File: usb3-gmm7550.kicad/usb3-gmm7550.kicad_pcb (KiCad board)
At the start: 4 copper layers, 75 x 50 mm, 209 parts, among them J1 USB_C_Receptacle, J2 USB_C_Receptacle_USB2.0, J3 SWD, J4 10144517-061802LF, J5 10144517-061802LF, J6 DNI, Q1 NX6008NBK, Q2 NX6008NBK, Q3 NX6008NBK, Q4 STL9P3LLH6, Q5 STL9P3LLH6, Q6 STL9P3LLH6, Q7 NX6008NBK, SW1 SW_Push, SW2 SW_Push, SW3 SW_Push, SW4 SW_Push, SW5 SW_Push, SW6 SW_DIP_x02, U1 ECMF4-40A100N10, U10 74LVC1G07, U11 INA180A2, U12 AP7330, U13 AP7330, U14 MX25R1635FZU, U15 ECMF02-2AMX6, U16 LM4040DBZ-3, U17 RP2040, U18 STUSB1600, U19 LM66200DRLR, U2 ECMF4-40A100N10, U3 ECMF02-2AMX6, U4 AP7330, U5 TUSB542, U6 SN65LVDS4RSER, U7 USB3340, U8 STUSB03E, U9 SiP32510, Y1 445I23D12M00000

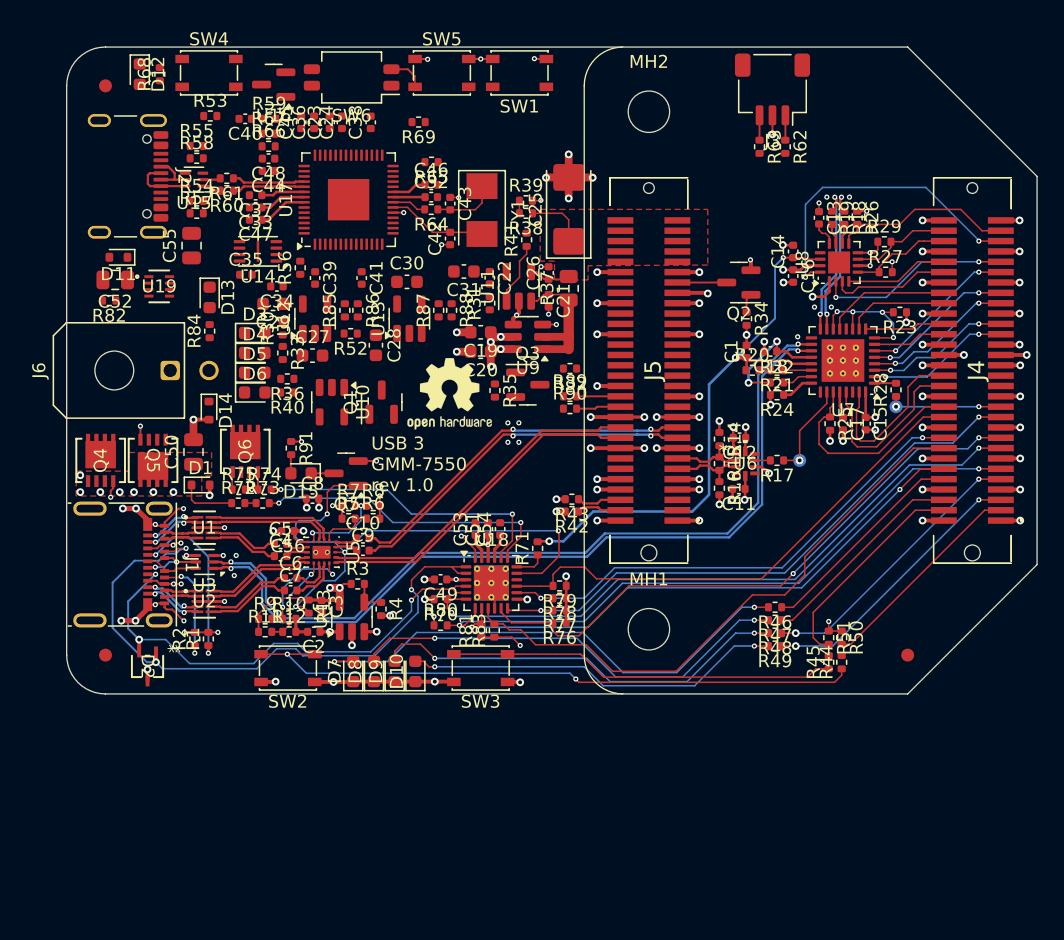
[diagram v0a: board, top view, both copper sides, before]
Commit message: USB Power Delivery redesign (STmicro controller is NRND)
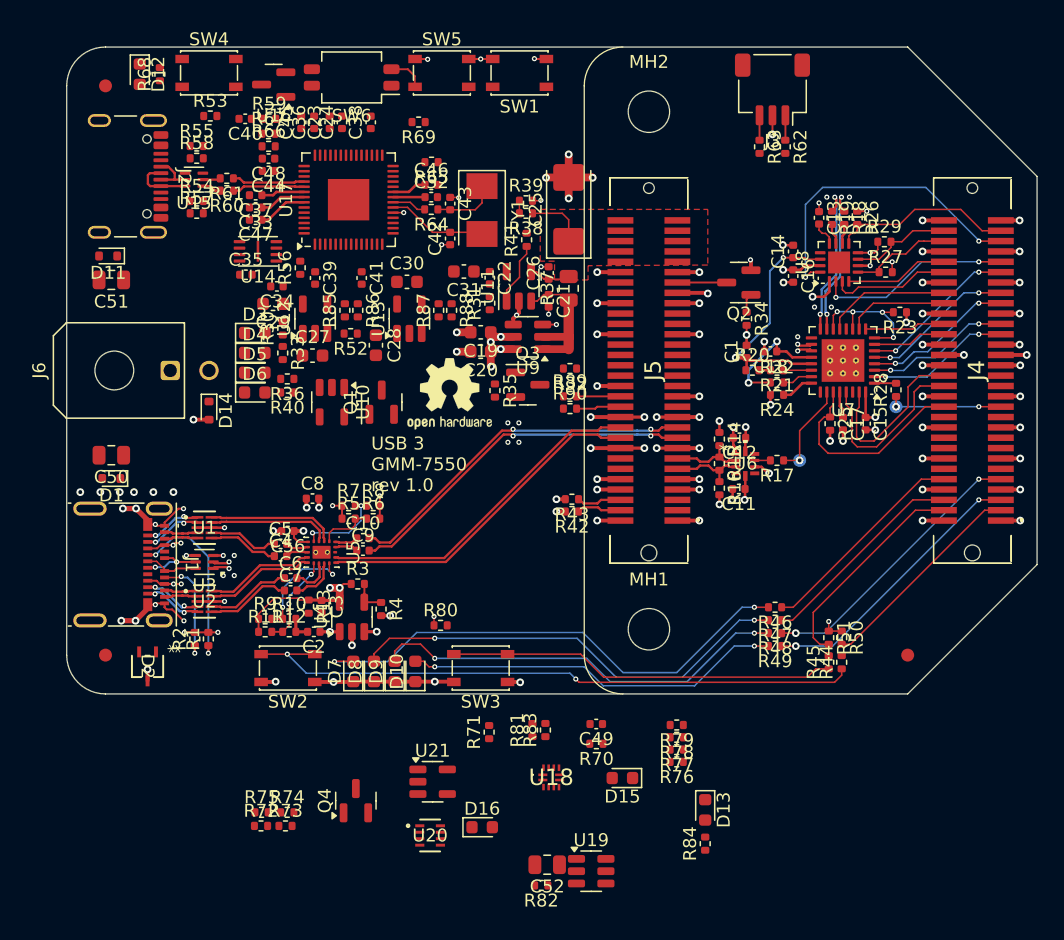
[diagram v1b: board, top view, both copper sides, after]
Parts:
- removed C53, C54: 1.0uF, Capacitor_SMD:C_0402_1005Metric
- removed C55: 10uF, Capacitor_SMD:C_0805_2012Metric
- removed Q5, Q6: STL9P3LLH6, usb3-gmm7550:POWERFLAT_3P3X3P3_STM
- removed Q7: NX6008NBK, Package_TO_SOT_SMD:SOT-23
- removed R91: 100, Resistor_SMD:R_0402_1005Metric
- added D16: 150060VS55040, LED_SMD:LED_0603_1608Metric, F.Cu at (92.1, 110.3)
- added U20: LM66200DRLR, usb3-gmm7550:SOT-5X3_DRL_TEX, F.Cu at (88.1, 110.9)
- added U21: 74LVC1G06, Package_TO_SOT_SMD:SOT-23-5, F.Cu at (88.3, 106.8)
- C51: value 1.0uF -> 10uF; footprint Capacitor_SMD:C_0402_1005Metric -> Capacitor_SMD:C_0805_2012Metric
- Q4: value STL9P3LLH6 -> NX6008NBK; footprint usb3-gmm7550:POWERFLAT_3P3X3P3_STM -> Package_TO_SOT_SMD:SOT-23
- R70: value 1k -> 10k
- R71: value 0 -> 10k
- R75: value 10k -> 1k
- R79: value 10k -> DNI
- R80: value 10k -> 0
- R81: value 10k -> 900k
- R82: value 0 -> 301
- R83: value 10k -> 100
- U18: value STUSB1600 -> FUSB303BTMX; footprint Package_DFN_QFN:QFN-24-1EP_4x4mm_P0.5mm_EP2.7x2.7mm_ThermalVias -> usb3-gmm7550:OnSemi_X2QFN-12_1.6x1.6mm
- U19: value LM66200DRLR -> SiP32508DT; footprint usb3-gmm7550:SOT-5X3_DRL_TEX -> Package_TO_SOT_SMD:TSOT-23-6
- moved C52 56.2 mm to (97.1, 113.2)
- moved R82 56.2 mm to (96.7, 114.8)
- moved U19 56.2 mm to (100.5, 113.7)
- moved D13 55.1 mm to (109.3, 109.0)
- moved R84 55.1 mm to (109.3, 111.6)
- moved C51 34.9 mm to (63.5, 68.0), turned to 180 degrees
- moved D15 34.2 mm to (103.0, 106.5)
- moved Q4 32.9 mm to (82.3, 108.2)
- moved R72 25.0 mm to (75.0, 110.2)
- moved R73 25.0 mm to (76.9, 110.2)
- moved R74 25.0 mm to (77.0, 109.2)
- moved R75 25.0 mm to (75.1, 109.2)
- moved C49 16.4 mm to (100.9, 102.3)
- moved R70 16.4 mm to (100.9, 103.8)
- moved U18 15.7 mm to (97.5, 106.5)
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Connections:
- C49 pad 1: +5V -> +3.3V
- C51 pad 1: +5V -> VBUS_INST
- C52 pad 1: VBUS_INST -> +5V
- D15 pad 1: Net-(D15-K) -> /USB PD/PD_SRC
- J4 pad 15: PD_RESET -> PD_EN_N
- Q4 pad 1: VBUS_TRGT -> PD_DIS
- Q4 pad 2: VBUS_TRGT -> GND
- Q4 pad 3: VBUS_TRGT -> Net-(Q4-D)
- R70 pad 1: PD_RESET -> PD_SRC_EN
- R71 pad 1: Net-(U18-VBUS_SENSE) -> VIO_2V5
- R71 pad 2: VBUS_TRGT -> PD_EN_N
- R72 pad 1: VBUS_TRGT -> PD_DIS
- R72 pad 2: Net-(Q4-G) -> GND
- R73 pad 1: Net-(Q4-G) -> VBUS_TRGT
- R73 pad 2: Net-(U18-VBUS_EN_SNK) -> Net-(Q4-D)
- R74 pad 1: Net-(Q5-G) -> VBUS_TRGT
- R74 pad 2: Net-(U18-VBUS_EN_SRC) -> Net-(Q4-D)
- R75 pad 1: Net-(Q5-S) -> VBUS_TRGT
- R75 pad 2: Net-(Q5-G) -> Net-(Q4-D)
- R76 pad 2: PD_VBUS_VALID -> PD_ALERT_N
- R77 pad 2: PD_ATTACH -> PD_SDA
- R78 pad 2: PD_DEBUG1 -> PD_SCL
- R79 pad 1: VIO_2V5 -> Net-(U18-PORT/DEBUG_N)
- R79 pad 2: PD_DEBUG2 -> GND
- R80 pad 1: VIO_2V5 -> Net-(U20-~{ON})
- R80 pad 2: PD_SCL -> GND
- R81 pad 1: VIO_2V5 -> GND
- R81 pad 2: PD_SDA -> Net-(U18-ADDR/ORIENT)
- R82 pad 1: Net-(U19-~{ON}) -> +5V
- R82 pad 2: GND -> Net-(D13-A)
- R83 pad 1: VIO_2V5 -> +3.3V
- R83 pad 2: PD_ALERT_N -> Net-(D15-A)
- R84 pad 2: Net-(D13-A) -> Net-(D16-A)
- U18 pad 11: PD_VBUS_VALID -> PD_EN_N
- U18 pad 12: PD_ATTACH -> +3.3V
- U18 pad 2: CON_CC1 -> CON_CC2
- U18 pad 3: +5V -> Net-(U18-PORT/DEBUG_N)
- U18 pad 4: CON_CC2 -> VBUS_TRGT
- U18 pad 5: CON_CC2 -> Net-(U18-ADDR/ORIENT)
- U18 pad 6: PD_RESET -> PD_ALERT_N
- U18 pad 7: PD_SCL -> PD_SDA
- U18 pad 8: PD_SDA -> PD_SCL
- U18 pad 9: PD_ALERT_N -> /USB PD/PD_SRC
- U19 pad 1: GND -> VBUS_TRGT
- U19 pad 2: +5V -> VBUS_TRGT
- U19 pad 3: VBUS_INST -> PD_SRC_EN
- U19 pad 4: Net-(U19-~{ON}) -> GND
- U19 pad 5: GND -> +5V
- U19 pad 6: Net-(Q4-D) -> +5V
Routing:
- net USB2_D_P: track 63.8 -> 2.45 mm
- net USB2_D_N: track 63.8 -> 2.45 mm
- net PD_RESET: track 50.6 -> 0.00 mm, vias 2 -> 0
- net PD_SCL: track 49.9 -> 0.00 mm, vias 2 -> 0
- net CON_CC1: track 48.7 -> 0.00 mm, vias 3 -> 0
- net PD_VBUS_VALID: track 46.4 -> 0.00 mm, vias 2 -> 0
- net PD_ALERT_N: track 45.6 -> 0.00 mm
- net PD_ATTACH: track 45.3 -> 0.00 mm, vias 2 -> 0
- net A_B_SIDE: track 43.8 -> 0.00 mm, vias 4 -> 0
- net PD_SDA: track 43.6 -> 0.00 mm, vias 2 -> 0
- net PD_DEBUG2: track 39.7 -> 0.00 mm
- net PD_DEBUG1: track 39.3 -> 0.00 mm, vias 2 -> 0
- net CON_CC2: track 38.5 -> 0.00 mm, vias 3 -> 0
- net VBUS_TRGT: track 57.7 -> 24.7 mm, vias 15 -> 12
- net Net-(U18-VBUS_EN_SNK): track 23.5 -> 0.00 mm, vias 2 -> 0
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- removed copper zone on F.Cu, net VBUS_TRGT

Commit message: Layout WIP: split power plane (internal layer 2)
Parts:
- added C53: 1.0uF, Capacitor_SMD:C_0402_1005Metric, F.Cu at (70.8, 82.2)
- moved C52 53.5 mm to (71.0, 66.5), turned to 90 degrees
- moved D13 53.5 mm to (72.9, 69.8), turned to 180 degrees
- moved R82 52.1 mm to (70.4, 69.8), turned to 0 degrees
- moved U20 48.0 mm to (67.2, 67.8)
- moved R84 47.1 mm to (72.5, 82.2), turned to -90 degrees
- moved U19 45.5 mm to (68.2, 81.7)
- moved R70 37.8 mm to (68.8, 84.0), turned to 0 degrees
- moved R80 33.3 mm to (66.9, 69.8)
- moved D16 33.0 mm to (71.8, 84.3)
- moved R72 32.0 mm to (78.0, 78.3), turned to 90 degrees
- moved Q4 29.3 mm to (75.5, 79.8), turned to -90 degrees
- moved R73 26.7 mm to (75.0, 83.6)
- moved R75 26.6 mm to (75.0, 82.6)
- moved R74 24.6 mm to (75.0, 84.6)
- moved D15 19.0 mm to (95.6, 89.0)
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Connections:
- D2 pad 1: CON_CC1 -> CON_CC2
- D2 pad 2: CON_CC2 -> CON_CC1
- J4 pad 17: PD_VBUS_VALID -> IO_SB_A5
- J4 pad 18: PD_DEBUG1 -> IO_SB_A1
- J4 pad 21: PD_ATTACH -> PD_SRC_EN
- J4 pad 22: PD_DEBUG2 -> PD_DISCH
- Q4 pad 1: PD_DIS -> PD_DISCH
- R72 pad 1: PD_DIS -> PD_DISCH
- U17 pad 35: IO_SB_A7 -> IO_SB_A5
- U17 pad 36: IO_SB_B7 -> IO_SB_A1
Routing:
- net VBUS_TRGT: track 24.7 -> 113.4 mm, vias 12 -> 15
- net GND: track 143.8 -> 220.9 mm, vias 110 -> 172
- net USB2_D_P: track 2.45 -> 65.7 mm
- net USB2_D_N: track 2.45 -> 65.7 mm
- net CON_CC2: track 0.00 -> 35.0 mm, vias 0 -> 3
- net CON_CC1: track 0.00 -> 34.0 mm, vias 0 -> 3
- net /RP2040/RP_LED_G: track 0.00 -> 25.3 mm, vias 0 -> 2
- net Net-(D16-K): track 0.00 -> 23.3 mm, vias 0 -> 2
- net +2V5: track 6.07 -> 28.1 mm, vias 0 -> 10
- net /RP2040/RP_QSPI_SS: track 0.00 -> 21.9 mm, vias 0 -> 2
- net +5V: track 6.36 -> 27.7 mm, vias 4 -> 14
- net +1V1: track 6.52 -> 22.9 mm, vias 0 -> 3
- net A_B_SIDE: track 0.00 -> 14.8 mm, vias 0 -> 3
- net +3.3V: track 3.37 -> 17.9 mm, vias 0 -> 8
- net Net-(D4-K): track 0.00 -> 14.1 mm, vias 0 -> 2
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- added copper zone on In2.Cu, net +2V5
- added copper zone on In2.Cu, net +3.3V
- added copper zone on In2.Cu, net +5V
- added copper zone on In2.Cu, net GND
- added copper zone on In2.Cu, net VBUS_INST
- added copper zone on In2.Cu, net VBUS_TRGT
- added copper zone on In2.Cu, net VIO_2V5

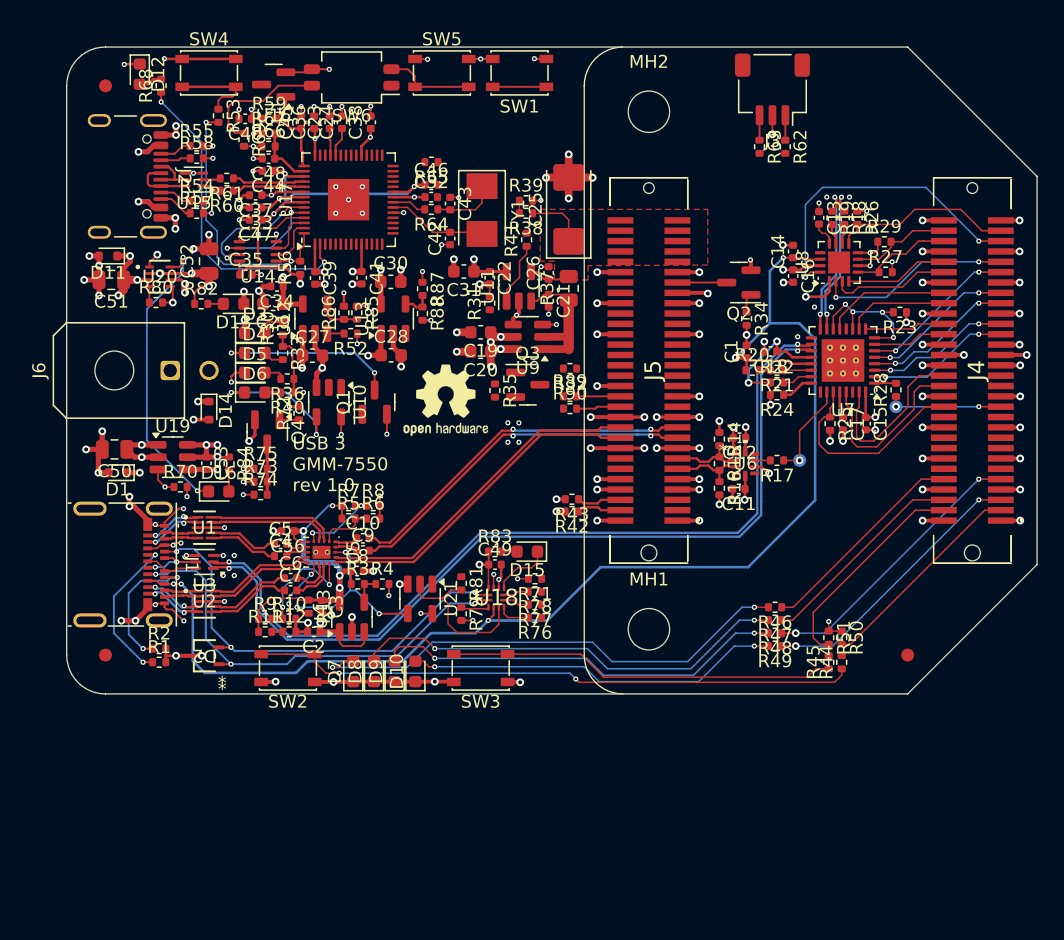
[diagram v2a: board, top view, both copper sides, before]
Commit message: Layout [almost] complete -- all connections are routed
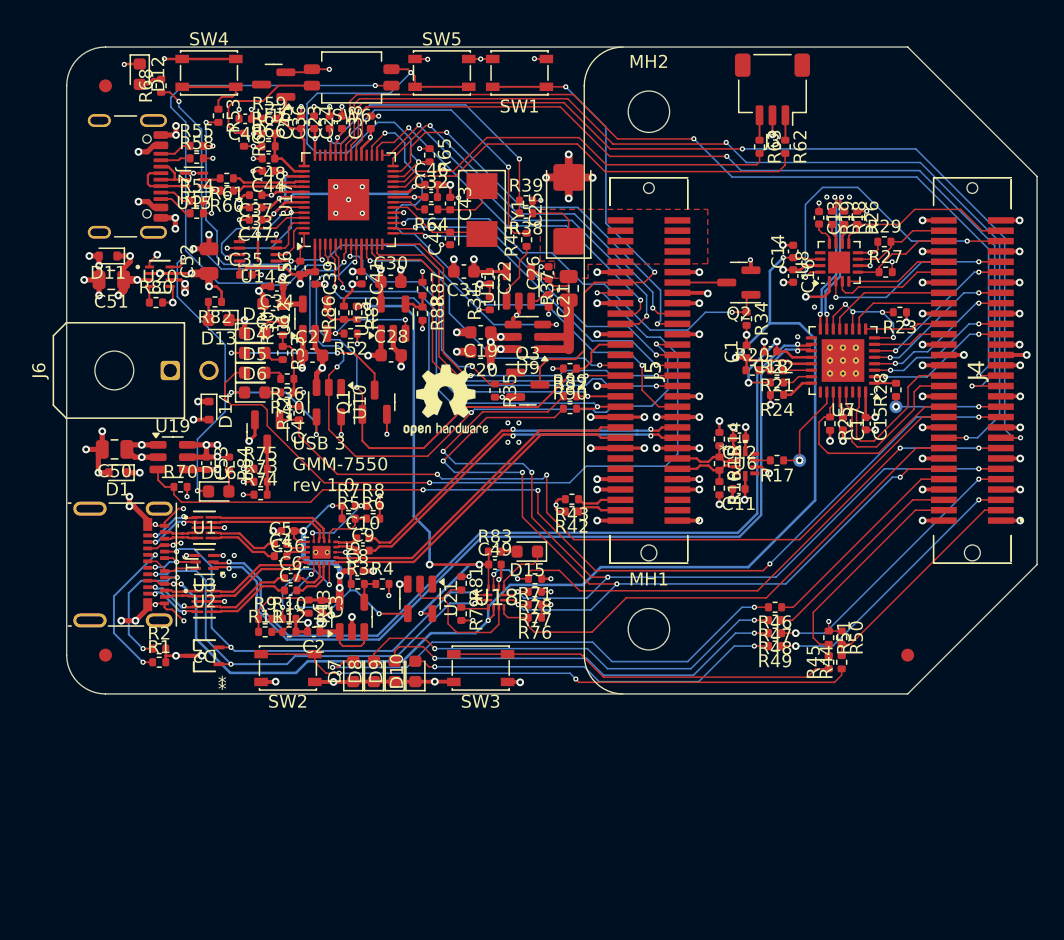
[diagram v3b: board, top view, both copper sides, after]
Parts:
- moved D13 1.70 mm to (71.8, 71.1)
- moved R82 1.07 mm to (71.5, 69.7), turned to 180 degrees
- moved R65 0.56 mm to (88.0, 58.4), turned to -90 degrees
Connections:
- J4 pad 27: unconnected-(J4-Pad27) -> IO_SB_B4
- J4 pad 29: unconnected-(J4-Pad29) -> IO_SB_A4
- U17 pad 18: M_RST -> unconnected-(U17-GPIO15-Pad18)
- U17 pad 32: CFG_NFAILED -> unconnected-(U17-GPIO21-Pad32)
- U17 pad 34: CFG_DONE -> IO_SB_B4
- U17 pad 37: unconnected-(U17-GPIO25-Pad37) -> IO_SB_A4
- U17 pad 7: unconnected-(U17-GPIO5-Pad7) -> CFG_NFAILED
- U17 pad 8: unconnected-(U17-GPIO6-Pad8) -> M_RST
- U17 pad 9: unconnected-(U17-GPIO7-Pad9) -> CFG_DONE
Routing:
- net IO_SB_A1: track 0.00 -> 77.4 mm, vias 0 -> 2
- net IO_SB_A5: track 0.00 -> 76.2 mm, vias 0 -> 2
- net PD_SRC_EN: track 2.26 -> 75.9 mm, vias 1 -> 4
- net PD_SCL: track 1.93 -> 73.5 mm, vias 0 -> 5
- net IO_SB_B4: track 0.00 -> 71.3 mm, vias 0 -> 2
- net IO_SB_A4: track 0.00 -> 70.8 mm, vias 0 -> 2
- net PD_SDA: track 1.97 -> 69.9 mm, vias 0 -> 5
- net PWR_EN: track 1.06 -> 67.1 mm, vias 1 -> 4
- net PD_DISCH: track 1.50 -> 61.8 mm, vias 0 -> 2
- net /GMM-7550/GMM_NRST: track 1.59 -> 60.0 mm, vias 1 -> 2
- net CFG_NFAILED: track 0.00 -> 53.5 mm, vias 0 -> 4
- net PD_EN_N: track 1.89 -> 46.4 mm, vias 2 -> 4
- net CFG_DONE: track 0.00 -> 43.2 mm, vias 0 -> 2
- net CLK25M: track 0.00 -> 41.1 mm, vias 0 -> 2
- net PD_ALERT_N: track 2.50 -> 41.4 mm
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
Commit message: Final touches -- revision 1.0 schematic is released
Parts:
- D2: value PESD752DCKR -> ESD752DCKR
- U10: value 74LVC1G07 -> SN74LVC1G07DBV
- U12, U13, U4: value AP7330 -> AP7330D
- U14: value MX25R1635FZU -> MX25R1635FZUIH0
- U16: value LM4040DBZ-3 -> LM4040A30IDBZ
- U21: value 74LVC1G06 -> SN74LVC1G06DBV
- moved R53 8.08 mm to (72.4, 63.4)
- moved D13 1.75 mm to (73.0, 69.8)
- moved R82 0.79 mm to (71.0, 70.3), turned to -90 degrees
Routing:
- net /RP2040/RP_QSPI_SS: track 21.9 -> 12.6 mm
- net Net-(R53-Pad1): track 6.91 -> 14.6 mm, vias 0 -> 2
- net Net-(U5-CNFG_A2): track 9.57 -> 7.95 mm
- net Net-(U5-CNFG_B2): track 7.16 -> 8.21 mm
- net IO_SB_A1: track 77.4 -> 76.7 mm
- net Net-(D13-A): track 1.41 -> 2.04 mm
- net +5V: track 27.4 -> 26.8 mm
- net VIO_2V5: track 50.8 -> 50.3 mm
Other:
- board text added: "0"
- board text added: "0 mm"
- board text added: "0.01 mm"
- board text added: "0.02"
- board text added: "0.035 mm"
- board text added: "0.1200 mm / 0.1200 mm"
- board text added: "0.14 mm"
- board text added: "0.2000 mm"
- board text added: "1"
- board text added: "1.2 mm"
- board text added: "1.6400 mm"
- board text added: "2"
- board text added: "3"
- board text added: "3.3"
- board text added: "4"
- board text added: "4.6"
- board text added: "75.0000 mm x 50.0000 mm"
- board text added: "90 Ohm ±10% differential impedance required on 0.18 mm traces/ 0.12 mm spacing on layers 1 and 4 (Top and Bottom)"
- board text added: "A"
- board text added: "B"
- board text added: "B.Cu"
- board text added: "B.Mask"
- board text added: "BOARD CHARACTERISTICS"
- board text added: "Black"
- board text added: "Board Thickness:"
- board text added: "Board overall dimensions:"
- board text added: "Boot"
- board text added: "Bottom Solder Mask"
- board text added: "Castellated pads:"
- board text added: "Color"
- board text added: "Copper Finish:"
- board text added: "Copper Layer Count:"
- board text added: "Dielectric"
- board text added: "ENIG"
- board text added: "Edge card connectors:"
- board text added: "Epsilon R"
- board text added: "F.Cu"
- board text added: "F.Mask"
- board text added: "F.Paste"
- board text added: "F.Silkscreen"
- board text added: "FR4"
- board text added: "GMM Reset"
- board text added: "Impedance Control:"
- board text added: "In1.Cu"
- board text added: "In2.Cu"
- board text added: "Layer Name"
- board text added: "Loss Tangent"
- board text added: "Material"
- board text added: "Min hole diameter:"
- board text added: "Min track/spacing:"
- board text added: "No"
- board text added: "Not specified"
- board text added: "Plated Board Edge:"
- board text added: "RP2040 Debug"
- board text added: "RPrst"
- board text added: "Thickness (mm)"
- board text added: "Top Silk Screen"
- board text added: "Top Solder Mask"
- board text added: "Top Solder Paste"
- board text added: "Type"
- board text added: "USB3 GMM-7550 rev 1.0"
- board text added: "White"
- board text added: "Yes"
- board text added: "copper"
- board text added: "core"
- board text added: "prepreg"
- board text removed: "USB 3 GMM-7550 rev 1.0"

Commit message: Final touches to the PCB, get ready to generate manufacturing files
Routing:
- net GND: track 228.8 -> 229.7 mm
- net PD_EN_N: track 46.4 -> 45.6 mm
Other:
- board text added: "RPreset"
- board text removed: "RPrst"
